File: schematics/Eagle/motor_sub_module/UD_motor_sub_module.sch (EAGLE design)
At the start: 2 parts, among them IC1 ULN2003AN

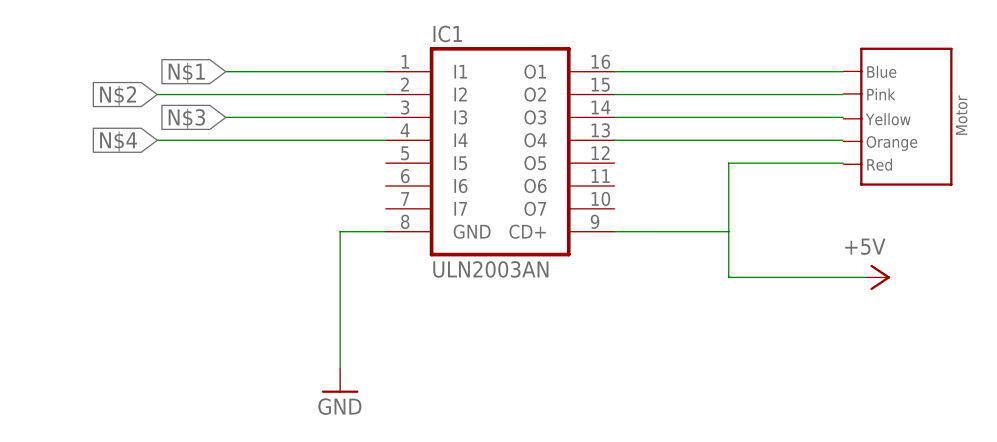
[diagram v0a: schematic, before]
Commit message: updated schematics with pinouts
Added pintout information for motors.
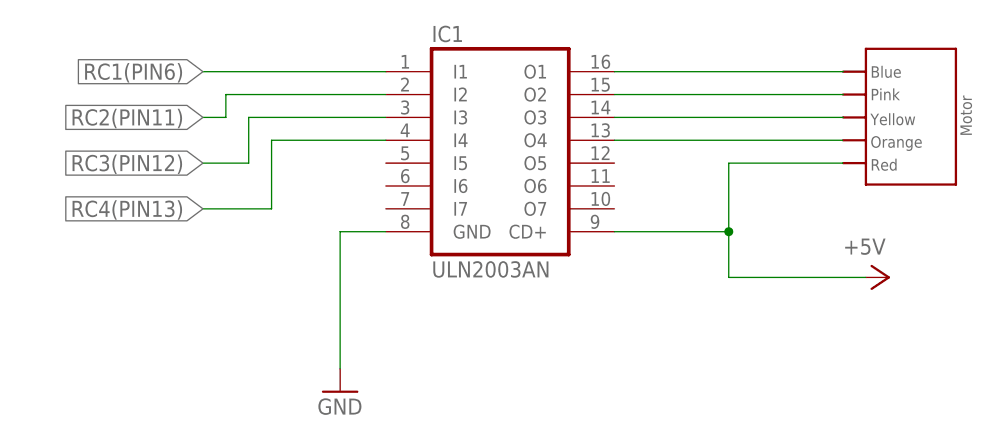
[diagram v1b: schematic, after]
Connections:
- net N$1 renamed RC1(PIN6)
- net N$2 renamed RC2(PIN11)
- net N$3 renamed RC3(PIN12)
- net N$4 renamed RC4(PIN13)
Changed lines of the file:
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@@
 <instances>
 <instance part="IC1" gate="A" x="66.04" y="63.5"/>
-<instance part="U$1" gate="G$1" x="106.172" y="71.12" rot="R270"/>
+<instance part="U$1" gate="G$1" x="106.68" y="71.12" rot="R270"/>
 <instance part="GND1" gate="1" x="48.26" y="35.56"/>
 <instance part="P+1" gate="1" x="109.22" y="48.26" rot="R270"/>
@@
 </busses>
 <nets>
-<net name="N$1" class="0">
-<segment>
-<pinref part="IC1" gate="A" pin="I1"/>
-<wire x1="53.34" y1="71.12" x2="35.56" y2="71.12" width="0.1524" layer="91"/>
-<label x="35.56" y="71.12" size="1.778" layer="95" rot="R180" xref="yes"/>
-</segment>
-</net>
-<net name="N$2" class="0">
-<segment>
-<pinref part="IC1" gate="A" pin="I2"/>
-<wire x1="53.34" y1="68.58" x2="27.94" y2="68.58" width="0.1524" layer="91"/>
-<label x="27.94" y="68.58" size="1.778" layer="95" rot="R180" xref="yes"/>
-</segment>
-</net>
-<net name="N$3" class="0">
-<segment>
-<pinref part="IC1" gate="A" pin="I3"/>
-<wire x1="53.34" y1="66.04" x2="35.56" y2="66.04" width="0.1524" layer="91"/>
-<label x="35.56" y="66.04" size="1.778" layer="95" rot="R180" xref="yes"/>
-</segment>
-</net>
-<net name="N$4" class="0">
-<segment>
-<pinref part="IC1" gate="A" pin="I4"/>
-<wire x1="53.34" y1="63.5" x2="27.94" y2="63.5" width="0.1524" layer="91"/>
-<label x="27.94" y="63.5" size="1.778" layer="95" rot="R180" xref="yes"/>
-</segment>
-</net>
 <net name="GND" class="0">
 <segment>
@@
 <wire x1="91.44" y1="53.34" x2="91.44" y2="48.26" width="0.1524" layer="91"/>
 <wire x1="91.44" y1="48.26" x2="106.68" y2="48.26" width="0.1524" layer="91"/>
+<junction x="91.44" y="53.34"/>
 </segment>
 </net>
@@
 </segment>
 </net>
+<net name="RC1(PIN6)" class="0">
+<segment>
+<pinref part="IC1" gate="A" pin="I1"/>
+<wire x1="53.34" y1="71.12" x2="33.02" y2="71.12" width="0.1524" layer="91"/>
+<label x="33.02" y="71.12" size="1.778" layer="95" rot="R180" xref="yes"/>
+</segment>
+</net>
+<net name="RC2(PIN11)" class="0">
+<segment>
+<pinref part="IC1" gate="A" pin="I2"/>
+<wire x1="53.34" y1="68.58" x2="35.56" y2="68.58" width="0.1524" layer="91"/>
+<wire x1="35.56" y1="68.58" x2="35.56" y2="66.04" width="0.1524" layer="91"/>
+<wire x1="35.56" y1="66.04" x2="33.02" y2="66.04" width="0.1524" layer="91"/>
+<label x="33.02" y="66.04" size="1.778" layer="95" rot="R180" xref="yes"/>
+</segment>
+</net>
+<net name="RC3(PIN12)" class="0">
+<segment>
+<pinref part="IC1" gate="A" pin="I3"/>
+<wire x1="53.34" y1="66.04" x2="38.1" y2="66.04" width="0.1524" layer="91"/>
+<wire x1="38.1" y1="66.04" x2="38.1" y2="60.96" width="0.1524" layer="91"/>
+<wire x1="38.1" y1="60.96" x2="33.02" y2="60.96" width="0.1524" layer="91"/>
+<label x="33.02" y="60.96" size="1.778" layer="95" rot="R180" xref="yes"/>
+</segment>
+</net>
+<net name="RC4(PIN13)" class="0">
+<segment>
+<pinref part="IC1" gate="A" pin="I4"/>
+<wire x1="53.34" y1="63.5" x2="40.64" y2="63.5" width="0.1524" layer="91"/>
+<wire x1="40.64" y1="63.5" x2="40.64" y2="55.88" width="0.1524" layer="91"/>
+<wire x1="40.64" y1="55.88" x2="33.02" y2="55.88" width="0.1524" layer="91"/>
+<label x="33.02" y="55.88" size="1.778" layer="95" rot="R180" xref="yes"/>
+</segment>
+</net>
